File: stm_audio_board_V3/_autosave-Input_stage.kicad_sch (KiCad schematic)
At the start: 92 parts, among them U4 OP275

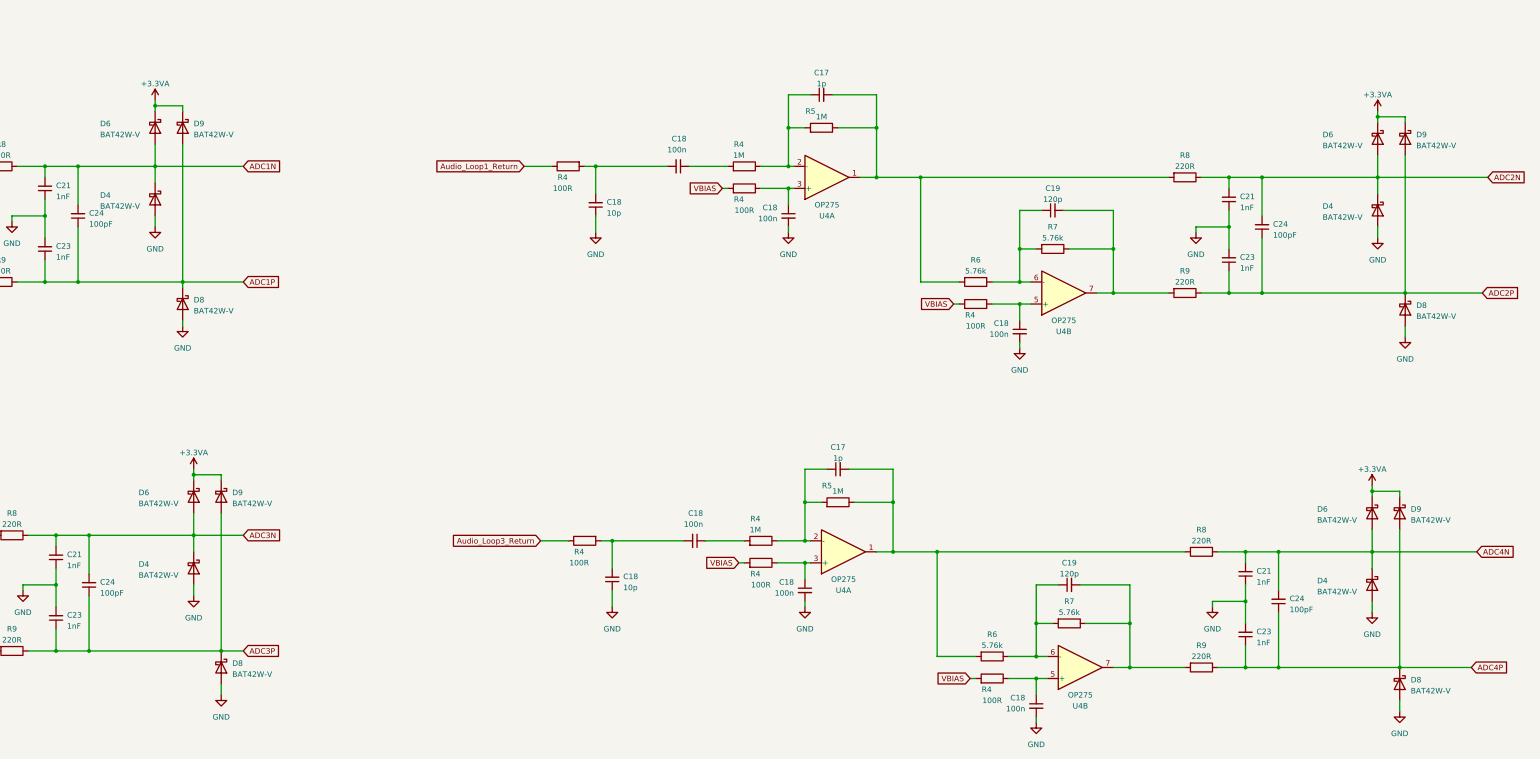
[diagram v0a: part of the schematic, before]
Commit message: Input output connected to codec
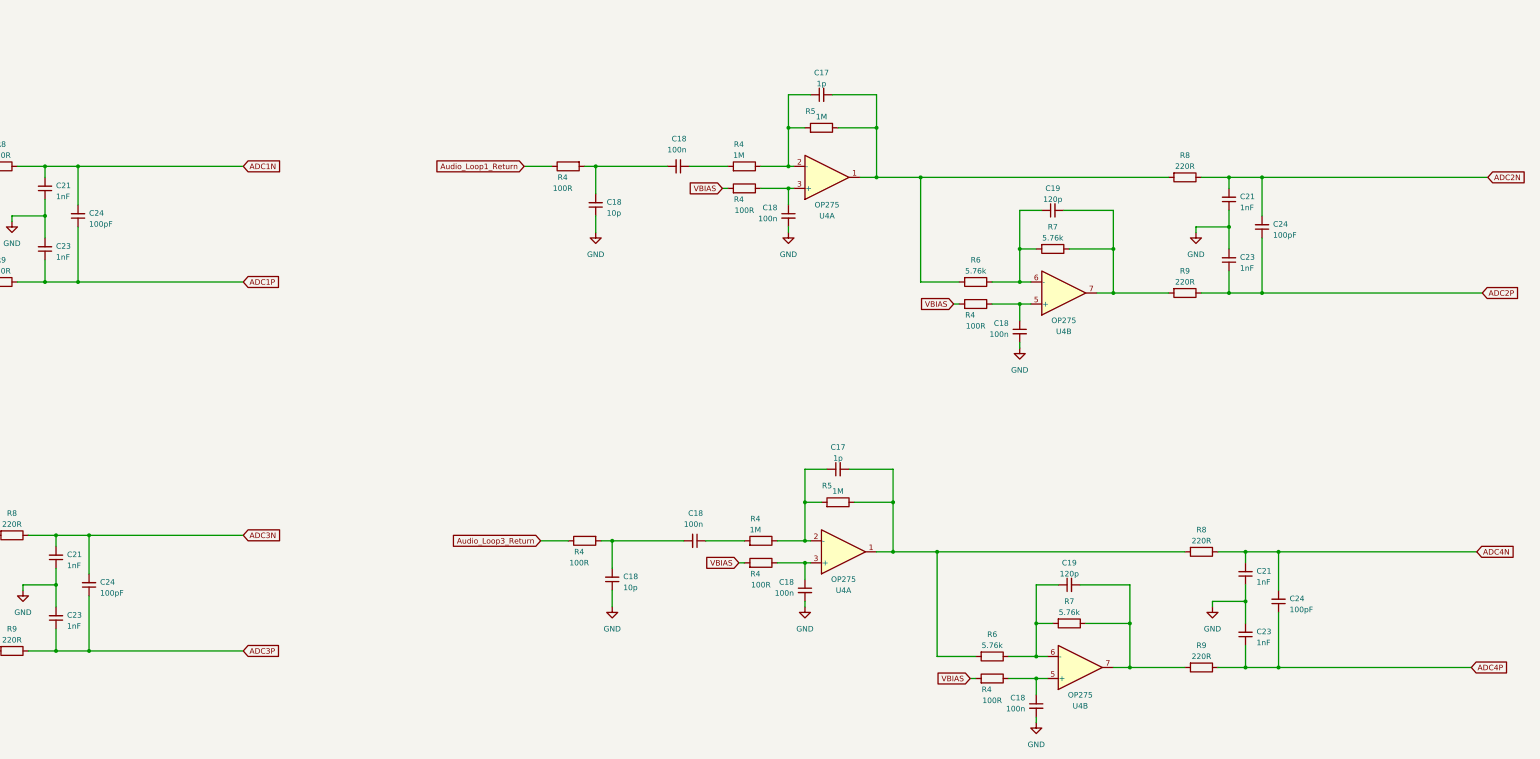
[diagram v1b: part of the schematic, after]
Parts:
- removed D4 (x4), D6 (x4), D8 (x4), D9 (x4): BAT42W-V, Diode_SMD:D_SOD-123, symbol Diode:BAT42W-V
